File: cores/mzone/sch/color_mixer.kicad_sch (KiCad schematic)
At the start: 18 parts

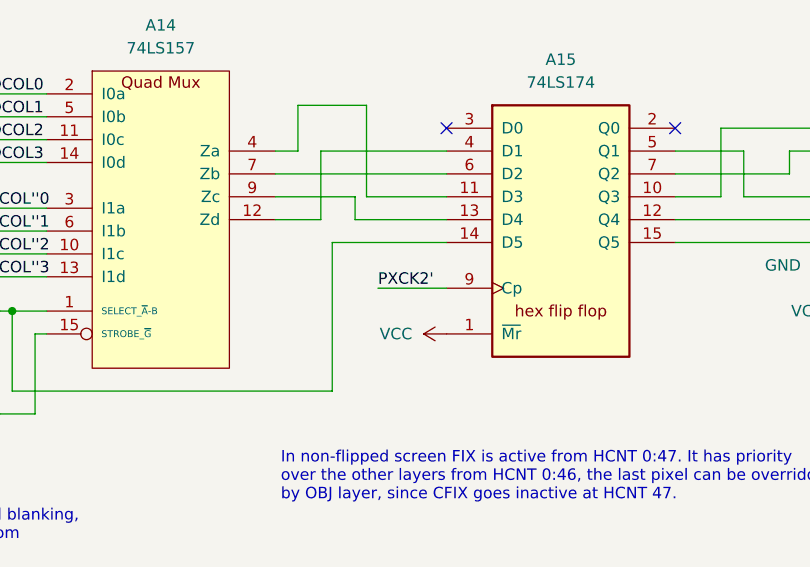
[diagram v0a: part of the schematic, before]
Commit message: mzone core
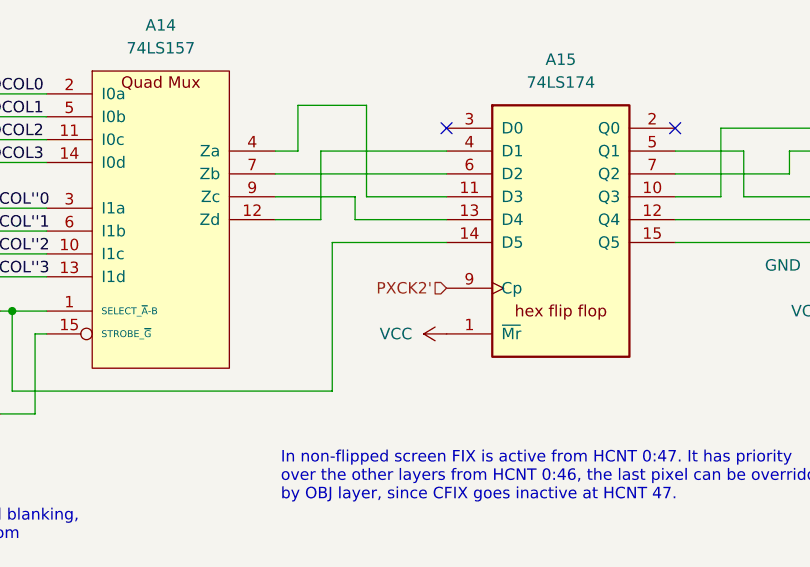
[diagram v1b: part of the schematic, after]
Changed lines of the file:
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@@
-	(wire
-		(pts
-			(xy 203.2 165.1) (xy 210.82 165.1)
-		)
-		(stroke
-			(width 0)
-			(type default)
-		)
-	)
 	(wire
 		(pts
@@
 		)
 	)
-	(label "PXCK2'"
-		(at 203.2 165.1 0)
-		(effects
-			(font
-				(size 1.27 1.27)
-			)
-			(justify left bottom)
-		)
-	)
 	(label "OCOL2"
 		(at 160.02 148.59 0)
@@
 		)
 	)
+	(hierarchical_label "PXCK2'"
+		(shape input)
+		(at 210.82 165.1 180)
+		(effects
+			(font
+				(size 1.27 1.27)
+			)
+			(justify right)
+		)
+	)

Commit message: mzone core
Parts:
- added unit 2 of A15
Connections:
- net GND: now also A15.8 (GND)
- net VCC: now also A15.16 (VCC); no longer A15.16 (VCC)
- removed net VSS: A15.8 (VSS)
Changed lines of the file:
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@@
+	)
+	(symbol
+		(lib_name "GND_1")
+		(lib_id "power:GND")
+		(at 278.13 278.13 0)
+		(unit 1)
+		(exclude_from_sim no)
+		(in_bom yes)
+		(on_board yes)
+		(dnp no)
+		(fields_autoplaced yes)
+		(property "Reference" "#PWR045"
+			(at 278.13 284.48 0)
+			(effects
+				(font
+					(size 1.27 1.27)
+				)
+				(hide yes)
+			)
+		)
+		(property "Value" "GND"
+			(at 278.13 283.21 0)
+			(effects
+				(font
+					(size 1.27 1.27)
+				)
+			)
+		)
+		(property "Footprint" ""
+			(at 278.13 278.13 0)
+			(effects
+				(font
+					(size 1.27 1.27)
+				)
+				(hide yes)
+			)
+		)
+		(property "Datasheet" ""
+			(at 278.13 278.13 0)
+			(effects
+				(font
+					(size 1.27 1.27)
+				)
+				(hide yes)
+			)
+		)
+		(property "Description" "Power symbol creates a global label with name \"GND\" , ground"
+			(at 278.13 278.13 0)
+			(effects
+				(font
+					(size 1.27 1.27)
+				)
+				(hide yes)
+			)
+		)
+		(pin "1"
+		)
+		(instances
+			(project ""
+				(path "/b3e039a8-74b0-4cb4-b612-5df1f0b42747/47e75e4f-6f19-40f9-a36d-bbd3cfcad077"
+					(reference "#PWR045")
+					(unit 1)
+				)
+			)
+		)
 	)
 	(symbol
@@
 	)
 	(symbol
+		(lib_name "VCC_1")
+		(lib_id "power:VCC")
+		(at 278.13 262.89 0)
+		(unit 1)
+		(exclude_from_sim no)
+		(in_bom yes)
+		(on_board yes)
+		(dnp no)
+		(fields_autoplaced yes)
+		(property "Reference" "#PWR044"
+			(at 278.13 266.7 0)
+			(effects
+				(font
+					(size 1.27 1.27)
+				)
+				(hide yes)
+			)
+		)
+		(property "Value" "VCC"
+			(at 278.13 257.81 0)
+			(effects
+				(font
+					(size 1.27 1.27)
+				)
+			)
+		)
+		(property "Footprint" ""
+			(at 278.13 262.89 0)
+			(effects
+				(font
+					(size 1.27 1.27)
+				)
+				(hide yes)
+			)
+		)
+		(property "Datasheet" ""
+			(at 278.13 262.89 0)
+			(effects
+				(font
+					(size 1.27 1.27)
+				)
+				(hide yes)
+			)
+		)
+		(property "Description" "Power symbol creates a global label with name \"VCC\""
+			(at 278.13 262.89 0)
+			(effects
+				(font
+					(size 1.27 1.27)
+				)
+				(hide yes)
+			)
+		)
+		(pin "1"
+		)
+		(instances
+			(project ""
+				(path "/b3e039a8-74b0-4cb4-b612-5df1f0b42747/47e75e4f-6f19-40f9-a36d-bbd3cfcad077"
+					(reference "#PWR044")
+					(unit 1)
+				)
+			)
+		)
+	)
+	(symbol
 		(lib_id "skutis_rom:PROM32W8B")
 		(at 264.16 157.48 0)
@@
 	)
 	(symbol
+		(lib_name "74LS174_1")
+		(lib_id "jt74:74LS174")
+		(at 278.13 270.51 0)
+		(unit 2)
+		(exclude_from_sim no)
+		(in_bom yes)
+		(on_board yes)
+		(dnp no)
+		(fields_autoplaced yes)
+		(property "Reference" "A15"
+			(at 284.48 269.2399 0)
+			(effects
+				(font
+					(size 1.27 1.27)
+				)
+				(justify left)
+			)
+		)
+		(property "Value" "74LS174"
+			(at 284.48 271.7799 0)
+			(effects
+				(font
+					(size 1.27 1.27)
+				)
+				(justify left)
+			)
+		)
+		(property "Footprint" ""
+			(at 278.13 270.51 0)
+			(effects
+				(font
+					(size 1.27 1.27)
+				)
+				(hide yes)
+			)
+		)
+		(property "Datasheet" "http://www.ti.com/lit/gpn/sn74LS174"
+			(at 279.4 289.56 0)
+			(effects
+				(font
+					(size 1.27 1.27)
+				)
+				(hide yes)
+			)
+		)
+		(property "Description" "Hex D-type Flip-Flop, reset"
+			(at 280.67 292.1 0)
+			(effects
+				(font
+					(size 1.27 1.27)
+				)
+				(hide yes)
+			)
+		)
+		(pin "6"
+		)
+		(pin "2"
+		)
+		(pin "14"
+		)
+		(pin "13"
+		)
+		(pin "12"
+		)
+		(pin "11"
+		)
+		(pin "10"
+		)
+		(pin "5"
+		)
+		(pin "1"
+		)
+		(pin "7"
+		)
+		(pin "8"
+		)
+		(pin "15"
+		)
+		(pin "4"
+		)
+		(pin "16"
+		)
+		(pin "9"
+		)
+		(pin "3"
+		)
+		(instances
+			(project ""
+				(path "/b3e039a8-74b0-4cb4-b612-5df1f0b42747/47e75e4f-6f19-40f9-a36d-bbd3cfcad077"
+					(reference "A15")
+					(unit 2)
+				)
+			)
+		)
+	)
+	(symbol
+		(lib_name "74LS174_1")
+		(lib_id "jt74:74LS174")
+		(at 223.52 157.48 0)
+		(unit 1)
+		(exclude_from_sim no)
+		(in_bom yes)
+		(on_board yes)
+		(dnp no)
+		(fields_autoplaced yes)
+		(property "Reference" "A15"
+			(at 223.52 139.7 0)
+			(effects
+				(font
+					(size 1.27 1.27)
+				)
+			)
+		)
+		(property "Value" "74LS174"
+			(at 223.52 142.24 0)
+			(effects
+				(font
+					(size 1.27 1.27)
+				)
+			)
+		)
+		(property "Footprint" ""
+			(at 223.52 157.48 0)
+			(effects
+				(font
+					(size 1.27 1.27)
+				)
+				(hide yes)
+			)
+		)
+		(property "Datasheet" "http://www.ti.com/lit/gpn/sn74LS174"
+			(at 224.79 176.53 0)
+			(effects
+				(font
+					(size 1.27 1.27)
+				)
+				(hide yes)
+			)
+		)
+		(property "Description" "Hex D-type Flip-Flop, reset"
+			(at 226.06 179.07 0)
+			(effects
+				(font
+					(size 1.27 1.27)
+				)
+				(hide yes)
+			)
+		)
+		(pin "6"
+		)
+		(pin "2"
+		)
+		(pin "14"
+		)
+		(pin "13"
+		)
+		(pin "12"
+		)
+		(pin "11"
+		)
+		(pin "10"
+		)
+		(pin "5"
+		)
+		(pin "1"
+		)
+		(pin "7"
+		)
+		(pin "8"
+		)
+		(pin "15"
+		)
+		(pin "4"
+		)
+		(pin "16"
+		)
+		(pin "9"
+		)
+		(pin "3"
+		)
+		(instances
+			(project ""
+				(path "/b3e039a8-74b0-4cb4-b612-5df1f0b42747/47e75e4f-6f19-40f9-a36d-bbd3cfcad077"
+					(reference "A15")
+					(unit 1)
+				)
+			)
+		)
+	)
+	(symbol
 		(lib_id "jt74:74LS10")
 		(at 153.67 179.07 0)
@@
 				)
 			)
-		)
-	)
-	(symbol
-		(lib_id "jt74:74LS174")
-		(at 223.52 157.48 0)
-		(unit 1)
-		(exclude_from_sim no)
-		(in_bom yes)
-		(on_board yes)
-		(dnp no)
-		(fields_autoplaced yes)
-		(property "Reference" "A15"
-			(at 223.52 139.7 0)
-			(effects
-				(font
-					(size 1.27 1.27)
-				)
-			)
-		)
-		(property "Value" "74LS174"
-			(at 223.52 142.24 0)
-			(effects
-				(font
-					(size 1.27 1.27)
-				)
-			)
-		)
-		(property "Footprint" ""
-			(at 223.52 157.48 0)
-			(effects
-				(font
-					(size 1.27 1.27)
-				)
-				(hide yes)
-			)
-		)
-		(property "Datasheet" "http://www.ti.com/lit/gpn/sn74LS174"
-			(at 224.79 176.53 0)
-			(effects
-				(font
-					(size 1.27 1.27)
-				)
-				(hide yes)
-			)
-		)
-		(property "Description" ""
-			(at 223.52 157.48 0)
-			(effects
-				(font
-					(size 1.27 1.27)
-				)
-				(hide yes)
-			)
-		)
-		(pin "9"
-		)
-		(pin "4"
-		)
-		(pin "5"
-		)
-		(pin "3"
-		)
-		(pin "8"
-		)
-		(pin "1"
-		)
-		(pin "14"
-		)
-		(pin "10"
-		)
-		(pin "11"
-		)
-		(pin "16"
-		)
-		(pin "15"
-		)
-		(pin "12"
-		)
-		(pin "2"
-		)
-		(pin "6"
-		)
-		(pin "7"
-		)
-		(pin "13"
-		)
-		(instances
-			(project "megazone"
-				(path "/b3e039a8-74b0-4cb4-b612-5df1f0b42747/47e75e4f-6f19-40f9-a36d-bbd3cfcad077"
-					(reference "A15")
-					(unit 1)
-				)
-			)

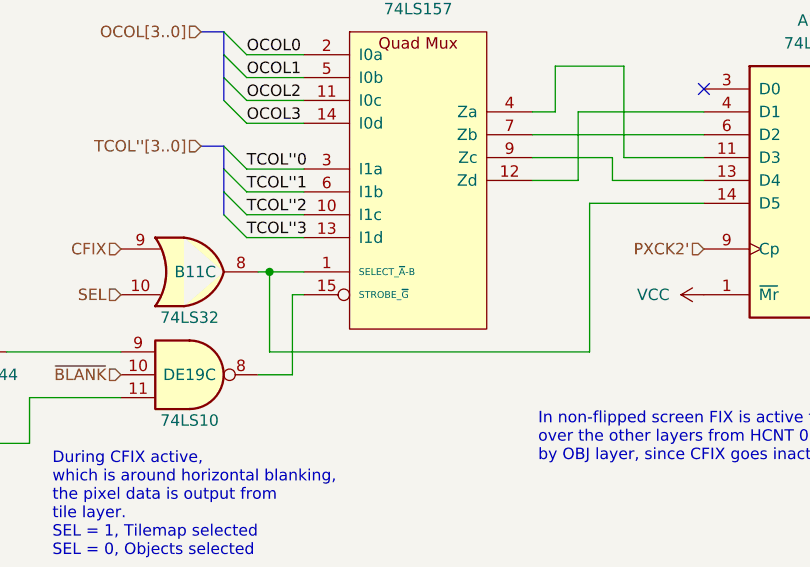
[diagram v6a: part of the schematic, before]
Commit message: mzone core
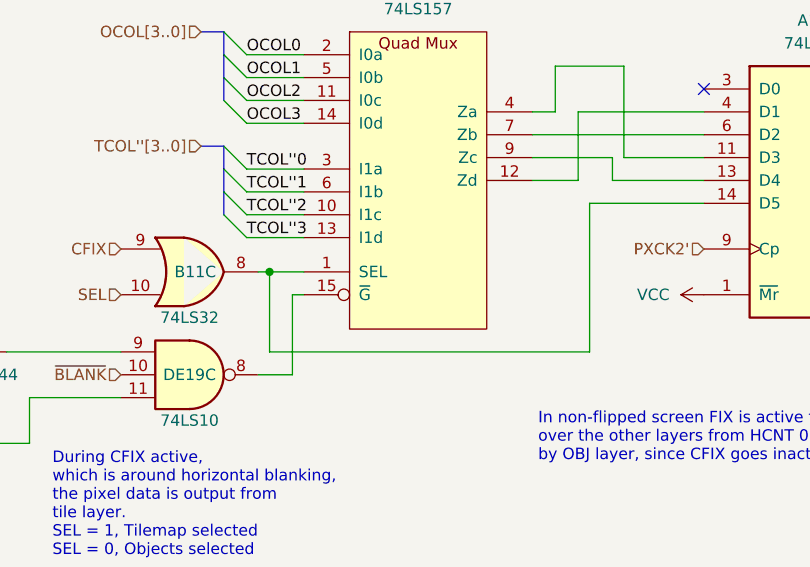
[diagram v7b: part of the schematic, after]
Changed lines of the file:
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@@
 	(label "R1"
 		(at 274.32 149.86 0)
+		(fields_autoplaced yes)
 		(effects
 			(font
@@
 	(label "OCOL0"
 		(at 160.02 143.51 0)
+		(fields_autoplaced yes)
 		(effects
 			(font
@@
 	(label "R0"
 		(at 274.32 147.32 0)
+		(fields_autoplaced yes)
 		(effects
 			(font
@@
 	(label "G2"
 		(at 274.32 160.02 0)
+		(fields_autoplaced yes)
 		(effects
 			(font
@@
 	(label "B0"
 		(at 274.32 162.56 0)
+		(fields_autoplaced yes)
 		(effects
 			(font
@@
 	(label "TCOL''2"
 		(at 160.02 161.29 0)
+		(fields_autoplaced yes)
 		(effects
 			(font
@@
 	(label "G2"
 		(at 276.86 132.08 0)
+		(fields_autoplaced yes)
 		(effects
 			(font
@@
 	(label "R0"
 		(at 276.86 119.38 0)
+		(fields_autoplaced yes)
 		(effects
 			(font
@@
 	(label "B1"
 		(at 276.86 137.16 0)
+		(fields_autoplaced yes)
 		(effects
 			(font
@@
 	(label "TCOL''3"
 		(at 160.02 163.83 0)
+		(fields_autoplaced yes)
 		(effects
 			(font
@@
 	(label "G1"
 		(at 276.86 129.54 0)
+		(fields_autoplaced yes)
 		(effects
 			(font
@@
 	(label "G0"
 		(at 276.86 127 0)
+		(fields_autoplaced yes)
 		(effects
 			(font
@@
 	(label "R2"
 		(at 276.86 124.46 0)
+		(fields_autoplaced yes)
 		(effects
 			(font
@@
 	(label "TCOL''1"
 		(at 160.02 158.75 0)
+		(fields_autoplaced yes)
 		(effects
 			(font
@@
 	(label "R1"
 		(at 276.86 121.92 0)
+		(fields_autoplaced yes)
 		(effects
 			(font
@@
 	(label "B1"
 		(at 274.32 165.1 0)
+		(fields_autoplaced yes)
 		(effects
 			(font
@@
 	(label "TCOL''0"
 		(at 160.02 156.21 0)
+		(fields_autoplaced yes)
 		(effects
 			(font
@@
 	(label "OCOL2"
 		(at 160.02 148.59 0)
+		(fields_autoplaced yes)
 		(effects
 			(font
@@
 	(label "B0"
 		(at 276.86 134.62 0)
+		(fields_autoplaced yes)
 		(effects
 			(font
@@
 	(label "R2"
 		(at 274.32 152.4 0)
+		(fields_autoplaced yes)
 		(effects
 			(font
@@
 	(label "OCOL1"
 		(at 160.02 146.05 0)
+		(fields_autoplaced yes)
 		(effects
 			(font
@@
 	(label "OCOL3"
 		(at 160.02 151.13 0)
+		(fields_autoplaced yes)
 		(effects
 			(font
@@
 	(label "G1"
 		(at 274.32 157.48 0)
+		(fields_autoplaced yes)
 		(effects
 			(font
@@
 	(label "G0"
 		(at 274.32 154.94 0)
+		(fields_autoplaced yes)
 		(effects
 			(font
@@
 		(shape input)
 		(at 154.94 140.97 180)
+		(fields_autoplaced yes)
 		(effects
 			(font
@@
 		(shape input)
 		(at 115.57 176.53 180)
+		(fields_autoplaced yes)
 		(effects
 			(font
@@
 		(shape output)
 		(at 300.99 167.64 0)
+		(fields_autoplaced yes)
 		(effects
 			(font
@@
 		(shape input)
 		(at 146.05 179.07 180)
+		(fields_autoplaced yes)
 		(effects
 			(font
@@
 		(shape input)
 		(at 146.05 170.18 180)
+		(fields_autoplaced yes)
 		(effects
 			(font
@@
 		(shape output)
 		(at 300.99 140.97 0)
+		(fields_autoplaced yes)
 		(effects
 			(font
@@
 		(shape input)
 		(at 210.82 165.1 180)
+		(fields_autoplaced yes)
 		(effects
 			(font
@@
 		(shape input)
 		(at 146.05 165.1 180)
+		(fields_autoplaced yes)
 		(effects
 			(font
@@
 		(shape input)
 		(at 154.94 153.67 180)
+		(fields_autoplaced yes)
 		(effects
 			(font
@@
 		(shape output)
 		(at 300.99 154.94 0)
+		(fields_autoplaced yes)
 		(effects
 			(font
@@
 	)
 	(symbol
-		(lib_name "GND_1")
 		(lib_id "power:GND")
 		(at 278.13 278.13 0)
@@
 	)
 	(symbol
-		(lib_name "GND_2")
 		(lib_id "power:GND")
 		(at 125.73 182.88 0)
@@
 			)
 		)
-		(property "Description" ""
+		(property "Description" "Power symbol creates a global label with name \"VCC\""
 			(at 210.82 170.18 0)
 			(effects
@@
 			)
 		)
-		(property "Description" ""
+		(property "Description" "Power symbol creates a global label with name \"GND\" , ground"
 			(at 295.91 162.56 0)
 			(effects
@@
 			)
 		)
-		(property "Datasheet" "https://www.alldatasheet.com/datasheet-pdf/pdf/27402/TI/74LS157.html"
+		(property "Datasheet" "https://www.ti.com/lit/ds/symlink/sn74ls157.pdf"
 			(at 179.07 175.26 0)
 			(effects
@@
 			)
 		)
-		(property "Description" ""
+		(property "Description" "Quad 2 to 1 line Multiplexer"
 			(at 179.07 156.21 0)
 			(effects
@@
 			)
 		)
-		(property "Description" ""
+		(property "Description" "Power symbol creates a global label with name \"VCC\""
 			(at 290.83 119.38 0)
 			(effects
@@
 			)
 		)
-		(property "Description" ""
+		(property "Description" "Power symbol creates a global label with name \"VCC\""
 			(at 256.54 167.64 0)
 			(effects
@@
 	)
 	(symbol
-		(lib_name "VCC_1")
 		(lib_id "power:VCC")
 		(at 278.13 262.89 0)
@@
 			)
 		)
-		(property "Description" ""
+		(property "Description" "Power symbol creates a global label with name \"GND\" , ground"
 			(at 295.91 149.86 0)
 			(effects
@@
 			)
 		)
-		(property "Description" ""
+		(property "Description" "Power symbol creates a global label with name \"GND\" , ground"
 			(at 254 162.56 0)
 			(effects
@@
 			)
 		)
-		(property "Description" ""
+		(property "Description" "Power symbol creates a global label with name \"GND\" , ground"
 			(at 295.91 175.26 0)
 			(effects
